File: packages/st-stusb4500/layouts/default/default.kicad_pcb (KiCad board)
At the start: 2 copper layers, 17 parts

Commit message: chore: Update packages for ato 0.10.7 (#69)
- Updates layouts with new net names due to https://github.com/atopile/atopile/pull/1226
- Disables failing DRCs
  - TODO: fix and re-enable for example/test/reference design builds that should be complete
  - TODO: make DRCs configurable and be more selective about what's disabled for "library" packages
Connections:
- net B6 renamed A6
- net DN2 renamed A7
- net SBU2 renamed B8
- net SSRXN2 renamed A10
- net SSRXP2 renamed A11
- net SSTXN2 renamed B3
- net SSTXP2 renamed B2
- net drain renamed anode
- net hv renamed -hv
- net line renamed -line-3
- net line-1 renamed -line-2
- net line-2 renamed -line-0
- net line-3 renamed -line-1
- net pd_controller-hv renamed pd_controller-hv-0

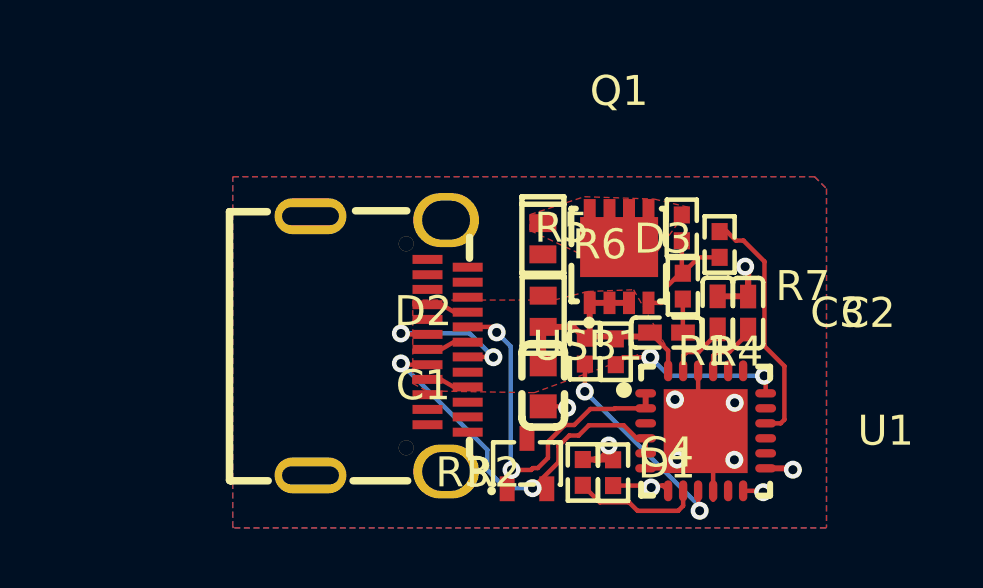
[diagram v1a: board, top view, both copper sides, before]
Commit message: convert to ato and fix layout
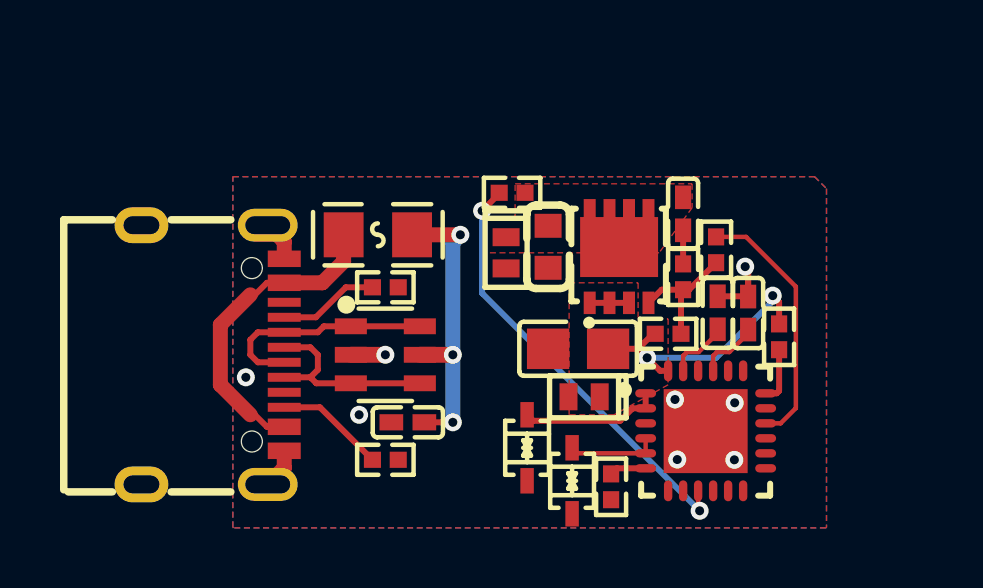
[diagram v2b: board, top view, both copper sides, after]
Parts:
- removed D2, D3: , STMicroelectronics_ESDA25P35_1U1M:DFN1610-2_L1.6-W1.0-P1.05-RD
- added C5: 1µF ±10% 50V X5R, Samsung_Electro_Mechanics_CL10A105KB8NNNC:C0603, F.Cu at (84.8, 68.2)
- added C6: 100nF ±10% 16V X7R, Samsung_Electro_Mechanics_CL05B104KO5NNNC:C0402, F.Cu at (89.3, 67.1)
- added F1: , BHFUSE_BSMD0805_050_15V:F0805, F.Cu at (79.1, 67.8)
- added R8: 100Ω ±1% 62.5mW, UNI_ROYAL_0402WGF1000TCE:R0402, F.Cu at (89.3, 69.2)
- added U2: , ElecSuper_CDSOD323_T24SC:SOD-323_L1.7-W1.3-LS2.7-BI, F.Cu at (85.6, 76.0)
- added U3: , STMicroelectronics_STUSB4500QTR:QFN-24_L4.0-W4.0-P0.50-BL-EP2.8, F.Cu at (90.1, 74.3)
- added U4: , STMicroelectronics_ESDA25P35_1U1M:DFN1610-2_L1.6-W1.0-P1.05-RD, F.Cu at (86.0, 73.2)
- added U5: , STMicroelectronics_ESDA25P35_1U1M:DFN1610-2_L1.6-W1.0-P1.05-RD, F.Cu at (83.4, 68.4)
- C1: value 4.7µF ±10% 35V X5R -> 1µF ±10% 25V X5R; footprint Murata_Electronics_GRM188R6YA475KE15D:C0603 -> Samsung_Electro_Mechanics_CL05A105KA5NQNC:C0402
- C3: value 1µF ±10% 25V X5R -> 100nF ±10% 16V X7R; footprint Samsung_Electro_Mechanics_CL05A105KA5NQNC:C0402 -> Samsung_Electro_Mechanics_CL05B104KO5NNNC:C0402
- C4: value 100nF ±10% 16V X7R -> 4.7µF ±10% 50V X5R; footprint Samsung_Electro_Mechanics_CL05B104KO5NNNC:C0402 -> Samsung_Electro_Mechanics_CL21A475KBQNNNE:C0805
- D1: footprint STMicroelectronics_ESDA25W:SOT-323-3_L2.1-W1.3-P1.32-LS2.1-BR -> STMicroelectronics_USBLC6_2SC6:SOT-23-6_L2.9-W1.6-P0.95-LS2.8-BL
- R1: value 1kΩ ±1% 62.5mW -> 10kΩ ±1% 62.5mW; footprint UNI_ROYAL_0402WGF1001TCE:R0402 -> UNI_ROYAL_0402WGF1002TCE:R0402
- R2, R3: value 4.7kΩ ±1% 62.5mW -> 5.1kΩ ±1% 62.5mW; footprint UNI_ROYAL_0402WGF4701TCE:R0402 -> UNI_ROYAL_0402WGF5101TCE:R0402
- R5: value 100kΩ ±1% 62.5mW -> 1kΩ ±1% 62.5mW; footprint UNI_ROYAL_0402WGF1003TCE:R0402 -> UNI_ROYAL_0402WGF1001TCE:R0402
- R6: value 22kΩ ±1% 62.5mW -> 100kΩ ±1% 62.5mW; footprint UNI_ROYAL_0402WGF2202TCE:R0402 -> UNI_ROYAL_0402WGF1003TCE:R0402
- R7: value 100Ω ±1% 62.5mW -> 22kΩ ±1% 62.5mW; footprint UNI_ROYAL_0402WGF1000TCE:R0402 -> UNI_ROYAL_0402WGF2202TCE:R0402
- U1: footprint STMicroelectronics_STUSB4500QTR:QFN-24_L4.0-W4.0-P0.50-BL-EP2.8 -> ElecSuper_CDSOD323_T24SC:SOD-323_L1.7-W1.3-LS2.7-BI
- USB1: footprint XKB_Connectivity_U262_241N_4BV64:USB-C-SMD_TYC-324G -> SHOU_HAN_TYPE_C_16PIN_2MD_073:USB-C-SMD_TYPE-C-6PIN-2MD-073
- moved C3 11.0 mm to (80.1, 74.0), turned to 180 degrees
- moved R2 9.79 mm to (79.4, 69.5), turned to 0 degrees
- moved R3 6.60 mm to (79.4, 75.3), turned to 0 degrees
- moved C1 6.30 mm to (90.5, 70.4)
- moved U1 5.98 mm to (84.1, 74.9)
- moved D1 5.95 mm to (79.4, 71.8)
- moved USB1 5.88 mm to (73.6, 71.8)
- moved R5 5.78 mm to (83.6, 66.4), turned to 180 degrees
- moved R4 5.47 mm to (92.5, 71.2)
- moved R1 4.61 mm to (86.9, 76.2)
- moved R6 3.44 mm to (88.8, 71.1), turned to 0 degrees
- moved C4 3.00 mm to (85.8, 71.6), turned to 0 degrees
- moved R7 1.64 mm to (90.4, 68.3), turned to 90 degrees
- turned C2 to 90 degrees
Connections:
- net usb_connector.footprint.pins[0].net-net renamed connector-net
- C1 pad 1: gnd -> power_2v7-VCC
- C1 pad 2: VBUS -> GND
- C2 pad 1: gnd -> power_1v2-VCC
- C2 pad 2: pd_controller-hv-0 -> GND
- C3 pad 1: gnd -> power_vbus-VCC
- C3 pad 2: pd_controller-hv-1 -> GND
- C4 pad 1: pd_controller-net -> GND
- C4 pad 2: VBUS -> power_vbus-VCC
- D1 pad 1: -line-2 -> USB_D_N
- D1 pad 2: -line-3 -> GND
- D1 pad 3: gnd -> USB_D_P
- Q1 pad 1: VBUS -> power_vbus-VCC
- Q1 pad 2: VBUS -> power_vbus-VCC
- Q1 pad 3: VBUS -> power_vbus-VCC
- Q1 pad 5: anode -> power_vsink-VCC
- Q1 pad 6: anode -> power_vsink-VCC
- Q1 pad 7: anode -> power_vsink-VCC
- Q1 pad 8: anode -> power_vsink-VCC
- Q1 pad 9: anode -> power_vsink-VCC
- R1 pad 1: VBUS -> RESET
- R1 pad 2: DISCH -> GND
- R2 pad 1: -line-0 -> cc[0]-anode
- R2 pad 2: -hv -> GND
- R3 pad 1: -line-1 -> cc[1]-anode
- R3 pad 2: -hv -> GND
- R4 pad 1: VBUS -> power_vbus-VCC
- R5 pad 1: gate -> power_vsink-VCC
- R5 pad 2: anode -> DISCH
- R6 pad 1: gate -> power_vbus-VCC
- R6 pad 2: VBUS_EN_SNK -> gate
- R7 pad 2: pd_controller-net -> VBUS_EN_SNK
- U1 pad 1: -line-2 -> cc[0]-anode
- U1 pad 2: -line-2 -> GND
- USB1 pad 1: gnd -> GND
- USB1 pad 2: gnd -> connector-power_vbus-VCC
- USB1 pad 3: gnd -> sbu[1]-line
- USB1 pad 4: gnd -> cc[0]-anode
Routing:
- net power_vbus-VCC: track 0.00 -> 20.9 mm, vias 0 -> 5
- net gnd: track 18.5 -> 0.00 mm, vias 6 -> 0
- net -line-3: track 13.0 -> 0.00 mm, vias 2 -> 0
- net -line-2: track 12.9 -> 0.00 mm, vias 2 -> 0
- net connector-power_vbus-VCC: track 0.00 -> 10.6 mm
- net VBUS: track 9.89 -> 0.00 mm
- net cc[0]-anode: track 0.00 -> 8.06 mm
- net USB_D_N: track 0.00 -> 7.57 mm
- net DISCH: track 7.17 -> 14.5 mm
- net GND: track 0.00 -> 6.83 mm, vias 0 -> 6
- net cc[1]-anode: track 0.00 -> 6.69 mm
- net USB_D_P: track 0.00 -> 6.68 mm
- net A7: track 5.17 -> 0.00 mm, vias 2 -> 0
- net -line-1: track 4.26 -> 0.00 mm
- net VBUS_VS_DISCH: track 5.91 -> 1.85 mm, vias 2 -> 0
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- added copper zone on B.Cu, net GND
- added copper zone on F.Cu, net GND
- added copper zone on F.Cu, net power_vbus-VCC
- added copper zone on F.Cu, net power_vsink-VCC
- removed copper zone on F.Cu, net VBUS
- removed copper zone on F.Cu, net anode
- removed copper zone on B.Cu, net gnd
- removed copper zone on F.Cu, net gnd

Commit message: ready for release
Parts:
- removed D1: , STMicroelectronics_USBLC6_2SC6:SOT-23-6_L2.9-W1.6-P0.95-LS2.8-BL
- removed F1: , BHFUSE_BSMD0805_050_15V:F0805
- removed R2, R3: 5.1kΩ ±1% 62.5mW, UNI_ROYAL_0402WGF5101TCE:R0402
- removed USB1: , SHOU_HAN_TYPE_C_16PIN_2MD_073:USB-C-SMD_TYPE-C-6PIN-2MD-073
- added Q2: , ALLPOWER_AP30P30Q:PDFN3333-8_L3.1-W3.2-P0.65-LS3.4-BL, F.Cu at (83.7, 71.6)
- C3: value 100nF ±10% 16V X7R -> 1µF ±10% 25V X5R; footprint Samsung_Electro_Mechanics_CL05B104KO5NNNC:C0402 -> Samsung_Electro_Mechanics_CL05A105KA5NQNC:C0402
- C4: value 4.7µF ±10% 50V X5R -> 2.2µF ±10% 50V X5R; footprint Samsung_Electro_Mechanics_CL21A475KBQNNNE:C0805 -> Samsung_Electro_Mechanics_CL10A225KB8NNNC:C0603
- moved C3 7.37 mm to (87.2, 72.0), turned to -90 degrees
- moved C4 4.38 mm to (83.3, 75.2), turned to 90 degrees
- moved U1 1.97 mm to (85.9, 74.1), turned to 180 degrees
- moved U4 1.20 mm to (86.0, 72.0), turned to -90 degrees
- moved R1 0.61 mm to (87.0, 76.8), turned to 180 degrees
- moved U2 0.41 mm to (85.7, 75.6), turned to 180 degrees
- moved R5 0.32 mm to (83.3, 66.5)
- moved C2 0.31 mm to (91.5, 70.1)
- moved C1 0.30 mm to (90.5, 70.1)
- moved R7 0.30 mm to (90.4, 68.0)
- moved C5 0.10 mm to (84.9, 68.2)
- moved U5 0.10 mm to (83.5, 68.4)
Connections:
- net cc[0]-anode renamed cc1-anode
- net cc[1]-anode renamed cc2-anode
- Q1 pad 1: power_vbus-VCC -> source
- Q1 pad 2: power_vbus-VCC -> source
- Q1 pad 3: power_vbus-VCC -> source
- R6 pad 1: power_vbus-VCC -> source
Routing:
- net connector-power_vbus-VCC: track 10.6 -> 0.00 mm
- net power_vbus-VCC: track 20.9 -> 11.8 mm, vias 5 -> 2
- net gate: track 4.31 -> 11.9 mm, vias 0 -> 2
- net USB_D_N: track 7.57 -> 0.00 mm
- net USB_D_P: track 6.68 -> 0.00 mm
- net cc1-anode: track 8.06 -> 1.77 mm
- net cc2-anode: track 6.69 -> 2.17 mm
- net GND: track 6.83 -> 2.83 mm, vias 6 -> 10
- net POWER_OK2: track 0.00 -> 1.63 mm, vias 0 -> 1
- net source: track 0.00 -> 1.38 mm
- net ALERT: track 0.00 -> 0.83 mm, vias 0 -> 1
- net DISCH: track 14.5 -> 15.3 mm
- net (no net): vias 2 -> 0
- added copper zone on F.Cu, net source

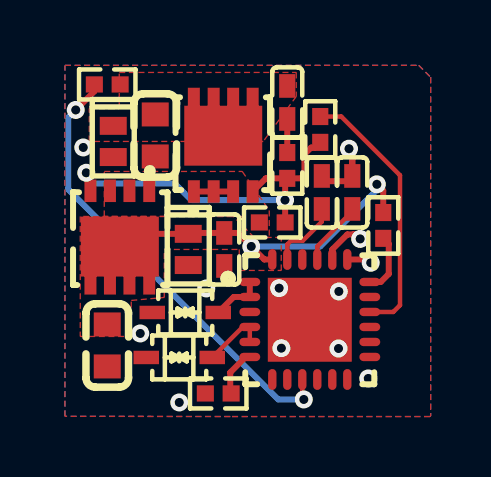
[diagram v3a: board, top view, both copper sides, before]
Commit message: st-stusb4500: package update to v0.3.0, ato:^0.14.0
Build targets:
  default = rc0
  stusb4500-usbc-connector = rc0
  usage = rc0
Package Verify: rc0
Version: 0.2.0 -> 0.3.0
Requires ato: ^0.14.0
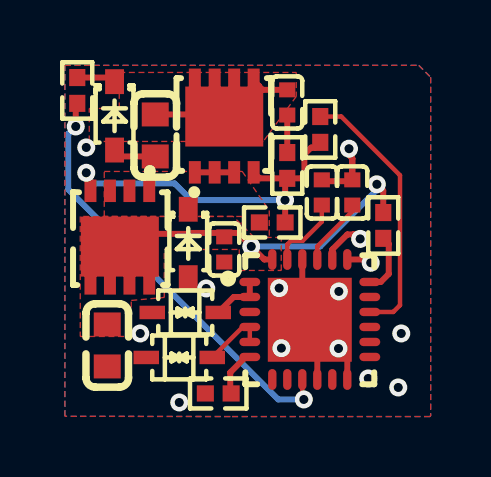
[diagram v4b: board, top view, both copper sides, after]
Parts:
- C1, C2, C3: value 1µF ±10% 25V X5R -> 1µF
- C4: value 2.2µF ±10% 50V X5R -> 2.2µF
- C5: value 1µF ±10% 50V X5R -> 1µF
- C6: value 100nF ±10% 16V X7R -> 100nF
- Q1, Q2: value (none) -> Vgs any ≥0V
- R1: value 10kΩ ±1% 62.5mW -> 10kΩ
- R4, R5: value 1kΩ ±1% 62.5mW -> 1kΩ
- R6: value 100kΩ ±1% 62.5mW -> 100kΩ
- R7: value 22kΩ ±1% 62.5mW -> 22kΩ
- R8: value 100Ω ±1% 62.5mW -> 100Ω
- U1, U2: value (none) -> Vf any ≥0V
- U4, U5: value (none) -> Vf any ≥0V; footprint STMicroelectronics_ESDA25P35_1U1M:DFN1610-2_L1.6-W1.0-P1.05-RD -> hongjiacheng_H12VHD3U:SOD-323_L1.7-W1.3-LS2.6-RD-1
- moved R5 1.02 mm to (82.3, 66.7), turned to -90 degrees
- moved U5 0.85 mm to (83.5, 67.5)
- moved Q1 0.64 mm to (87.2, 67.9)
- moved U4 0.20 mm to (86.0, 71.8)
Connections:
- net POWER_OK2 renamed 20
- net POWER_OK3 renamed 14
- net footprint-net-1 renamed vsink_gate_snub_c-power-hv
- net power_1v2-VCC renamed decoupling_caps[1]-power-hv
- net power_2v7-VCC renamed hv
- net power_vbus-VCC renamed cathode
- net power_vsink-VCC renamed vsink_gate_snub_c-power-cathode
- C1 pad 2: GND -> anode
- C2 pad 2: GND -> anode
- C3 pad 2: GND -> anode
- C4 pad 1: GND -> anode
- C5 pad 1: GND -> anode
- R1 pad 2: GND -> anode
- U1 pad 2: GND -> anode
- U2 pad 2: GND -> anode
- U3 pad 10: GND -> anode
- U3 pad 12: address_bit_0 -> anode
- U3 pad 13: address_bit_1 -> anode
- U3 pad 22: GND -> anode
- U3 pad 25: GND -> anode
- U3 pad 3: footprint-net-0 -> (no net)
- U4 pad 2: GND -> anode
- U5 pad 2: GND -> anode
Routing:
- net anode: track 0.00 -> 11.0 mm, vias 0 -> 11
- net vsink_gate_snub_c-power-cathode: track 0.00 -> 5.05 mm
- net GND: track 2.83 -> 0.00 mm, vias 10 -> 0
- net DISCH: track 15.3 -> 14.5 mm
- net (no net): vias 0 -> 1
- added copper zone on B.Cu, net anode
- added copper zone on F.Cu, net anode
- removed copper zone on B.Cu, net GND
- removed copper zone on F.Cu, net GND

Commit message: updatae layouts
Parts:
- removed U4, U5: Vf any ≥0V, hongjiacheng_H12VHD3U:SOD-323_L1.7-W1.3-LS2.6-RD-1
- added D1: , STMicroelectronics_ESDA25P35_1U1M:DFN1610-2_L1.6-W1.0-P1.05-RD, F.Cu at (0.00, 0.00)
- added D2: , STMicroelectronics_ESDA25P35_1U1M:DFN1610-2_L1.6-W1.0-P1.05-RD, F.Cu at (10.0, 0.00)
- U1, U2: value Vf any ≥0V -> (none)
- moved R5 1.02 mm to (83.3, 66.5), turned to 180 degrees
- moved Q1 0.64 mm to (87.2, 68.5)
- turned U1 to 0 degrees
- turned U2 to 0 degrees
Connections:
- net cathode renamed vbus_cap-power-hv
- C1 pad 1: hv -> decoupling_caps[0]-power-hv
- C1 pad 2: anode -> hv
- C2 pad 2: anode -> hv
- C3 pad 2: anode -> hv
- C4 pad 1: anode -> hv
- C5 pad 1: anode -> hv
- C5 pad 2: vsink_gate_snub_c-power-cathode -> vsink_gate_snub_c-power-hv
- C6 pad 1: vsink_gate_snub_c-power-hv -> vsink_gate_snub_c-power-hv-1
- C6 pad 2: vsink_gate_snub_c-power-cathode -> vsink_gate_snub_c-power-hv
- Q1 pad 5: vsink_gate_snub_c-power-cathode -> vsink_gate_snub_c-power-hv
- Q1 pad 6: vsink_gate_snub_c-power-cathode -> vsink_gate_snub_c-power-hv
- Q1 pad 7: vsink_gate_snub_c-power-cathode -> vsink_gate_snub_c-power-hv
- Q1 pad 8: vsink_gate_snub_c-power-cathode -> vsink_gate_snub_c-power-hv
- Q1 pad 9: vsink_gate_snub_c-power-cathode -> vsink_gate_snub_c-power-hv
- R1 pad 2: anode -> hv
- R5 pad 1: vsink_gate_snub_c-power-cathode -> vsink_gate_snub_c-power-hv
- R8 pad 2: vsink_gate_snub_c-power-hv -> vsink_gate_snub_c-power-hv-1
- U1 pad 1: cc1-anode -> hv
- U1 pad 2: anode -> CC1DB
- U2 pad 1: cc2-anode -> hv
- U2 pad 2: anode -> CC2DB
- U3 pad 1: cc1-anode -> CC1DB
- U3 pad 10: anode -> hv
- U3 pad 12: anode -> hv
- U3 pad 13: anode -> hv
- U3 pad 2: cc1-anode -> CC1DB
- U3 pad 22: anode -> hv
- U3 pad 23: hv -> decoupling_caps[0]-power-hv
- U3 pad 25: anode -> hv
- U3 pad 4: cc2-anode -> CC2DB
- U3 pad 5: cc2-anode -> CC2DB
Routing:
- net anode: track 11.0 -> 0.00 mm, vias 11 -> 0
- net vsink_gate_snub_c-power-cathode: track 5.05 -> 0.00 mm
- net 18: track 0.00 -> 2.83 mm, vias 0 -> 10
- net hv: track 2.39 -> 0.00 mm
- net decoupling_caps[0]-power-hv: track 0.00 -> 2.39 mm
- net cc2-anode: track 2.17 -> 0.00 mm
- net CC2DB: track 0.00 -> 2.17 mm
- net cc1-anode: track 1.77 -> 0.00 mm
- net CC1DB: track 0.00 -> 1.77 mm
- net vsink_gate_snub_c-power-hv-1: track 0.00 -> 1.12 mm
- net vsink_gate_snub_c-power-hv: track 1.12 -> 0.00 mm
- net DISCH: track 14.5 -> 15.3 mm
- net (no net): vias 1 -> 0
- added copper zone on B.Cu, net GND
- added copper zone on F.Cu, net GND
- added copper zone on F.Cu, net vsink_gate_snub_c-power-hv
- removed copper zone on B.Cu, net anode
- removed copper zone on F.Cu, net anode
- removed copper zone on F.Cu, net vsink_gate_snub_c-power-cathode

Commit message: fix pours and connections
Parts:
- C1, C2, C3, C5: value 1µF -> 0F
- C4: value 2.2µF -> 0F
- C6: value 100nF -> 0F
- Q1, Q2: value Vgs any ≥0V -> Vgs ℝ+V
- R1: value 10kΩ -> 10000Ω
- R4, R5: value 1kΩ -> 1000Ω
- R6: value 100kΩ -> 100000Ω
- R7: value 22kΩ -> 22000Ω
- moved D1 112.2 mm to (86.0, 72.0), turned to -90 degrees
- moved D2 100.3 mm to (83.5, 68.3), turned to -90 degrees
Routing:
- net hv: track 0.00 -> 2.83 mm, vias 0 -> 10
- net 18: track 2.83 -> 0.00 mm, vias 10 -> 0
- added copper zone on B.Cu, net hv
- added copper zone on F.Cu, net hv
- removed copper zone on B.Cu, net GND
- removed copper zone on F.Cu, net GND

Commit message: remove deprecated parts
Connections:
- net CC1DB renamed cathode
- net CC2DB renamed cc2-cathode
- net vbus_cap-power-hv renamed vbus_cap-power-cathode
- C1 pad 1: decoupling_caps[0]-power-hv -> hv
- C1 pad 2: hv -> anode
- C2 pad 2: hv -> anode
- C3 pad 2: hv -> anode
- C4 pad 1: hv -> anode
- C5 pad 1: hv -> anode
- C5 pad 2: vsink_gate_snub_c-power-hv -> vsink_gate_snub_c-power-cathode
- C6 pad 1: vsink_gate_snub_c-power-hv-1 -> vsink_gate_snub_c-power-hv
- C6 pad 2: vsink_gate_snub_c-power-hv -> vsink_gate_snub_c-power-cathode
- D1 pad 2: hv -> anode
- D2 pad 1: vsink_gate_snub_c-power-hv -> vsink_gate_snub_c-power-cathode
- D2 pad 2: hv -> anode
- Q1 pad 5: vsink_gate_snub_c-power-hv -> vsink_gate_snub_c-power-cathode
- Q1 pad 6: vsink_gate_snub_c-power-hv -> vsink_gate_snub_c-power-cathode
- Q1 pad 7: vsink_gate_snub_c-power-hv -> vsink_gate_snub_c-power-cathode
- Q1 pad 8: vsink_gate_snub_c-power-hv -> vsink_gate_snub_c-power-cathode
- Q1 pad 9: vsink_gate_snub_c-power-hv -> vsink_gate_snub_c-power-cathode
- R1 pad 2: hv -> anode
- R5 pad 1: vsink_gate_snub_c-power-hv -> vsink_gate_snub_c-power-cathode
- R8 pad 2: vsink_gate_snub_c-power-hv-1 -> vsink_gate_snub_c-power-hv
- U1 pad 1: hv -> anode
- U2 pad 1: hv -> anode
- U3 pad 10: hv -> anode
- U3 pad 12: hv -> anode
- U3 pad 13: hv -> anode
- U3 pad 22: hv -> anode
- U3 pad 23: decoupling_caps[0]-power-hv -> hv
- U3 pad 25: hv -> anode
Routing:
- net anode: track 0.00 -> 2.83 mm, vias 0 -> 10
- net decoupling_caps[0]-power-hv: track 2.39 -> 0.00 mm
- net vsink_gate_snub_c-power-hv-1: track 1.12 -> 0.00 mm
- net vsink_gate_snub_c-power-hv: track 0.00 -> 1.12 mm
- net hv: track 2.83 -> 2.39 mm, vias 10 -> 0
- added copper zone on B.Cu, net anode
- added copper zone on F.Cu, net anode
- added copper zone on F.Cu, net vsink_gate_snub_c-power-cathode
- removed copper zone on B.Cu, net hv
- removed copper zone on F.Cu, net hv
- removed copper zone on F.Cu, net vsink_gate_snub_c-power-hv
